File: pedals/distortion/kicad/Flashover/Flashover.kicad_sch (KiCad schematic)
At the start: 0 parts

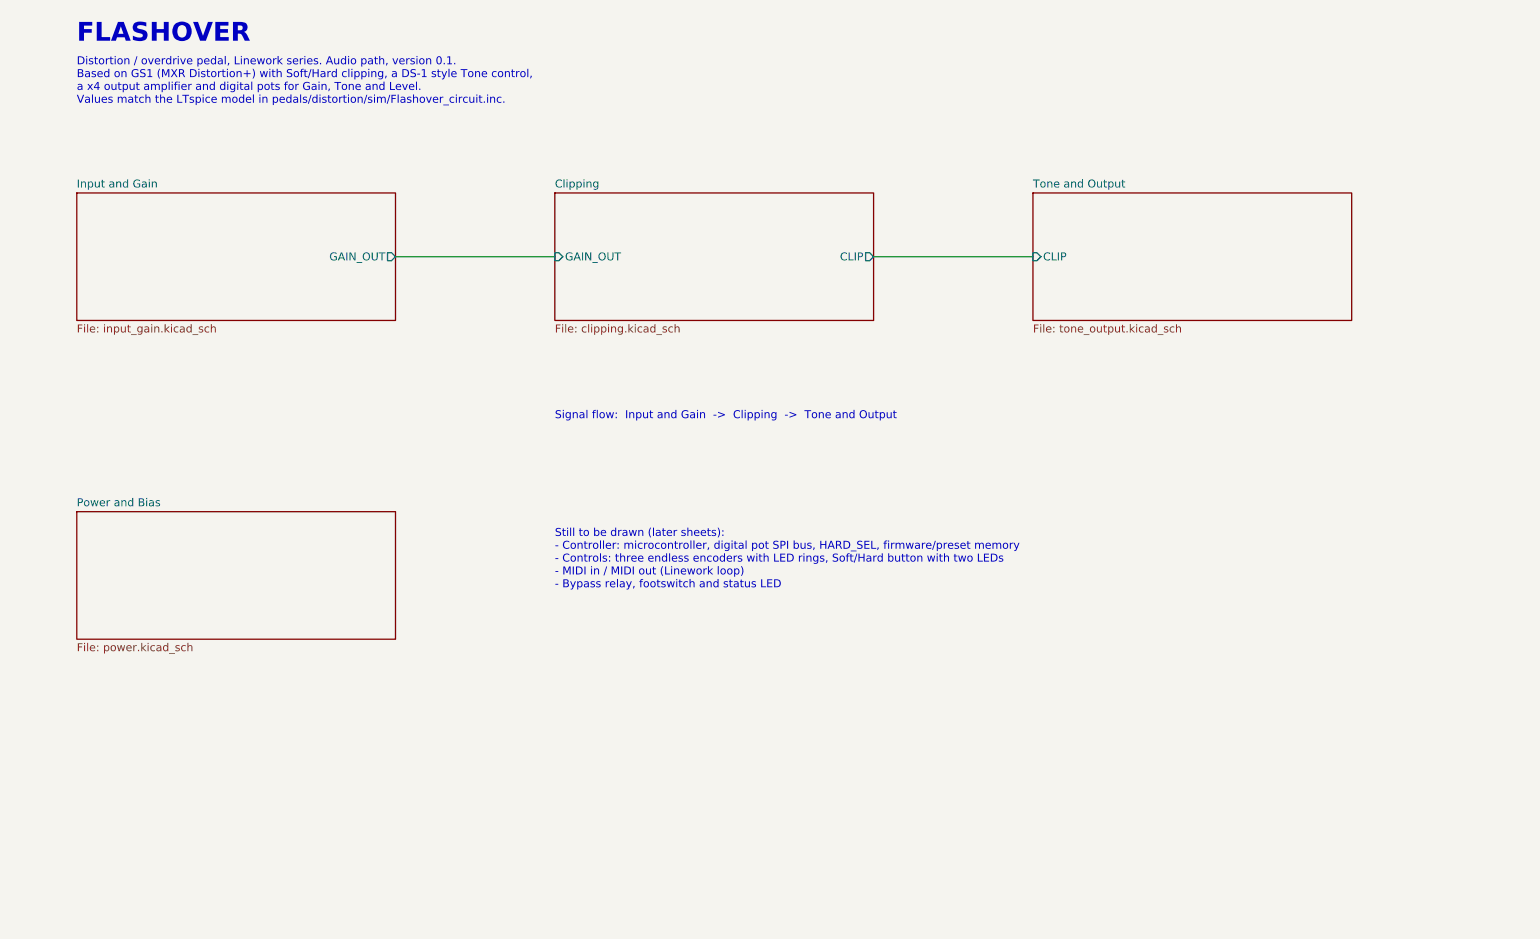
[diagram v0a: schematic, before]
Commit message: Add Flashover controller and digital pot sheets
Controller sheet: RP2040 with 3.3V regulator, 2 MB QSPI flash, 12 MHz
crystal and SWD header, plus a GPIO plan for the sheets still to come.
Digital Pots sheet: control side of three MCP45HV51 I2C pots with
pull-ups. RV1-RV3 on the audio sheets become the pot units of U7-U9
(new two-unit MCP45HV51 symbol in the shared library). ERC clean.

Co-Authored-By: Claude Opus 5.5 <noreply@anthropic.com>
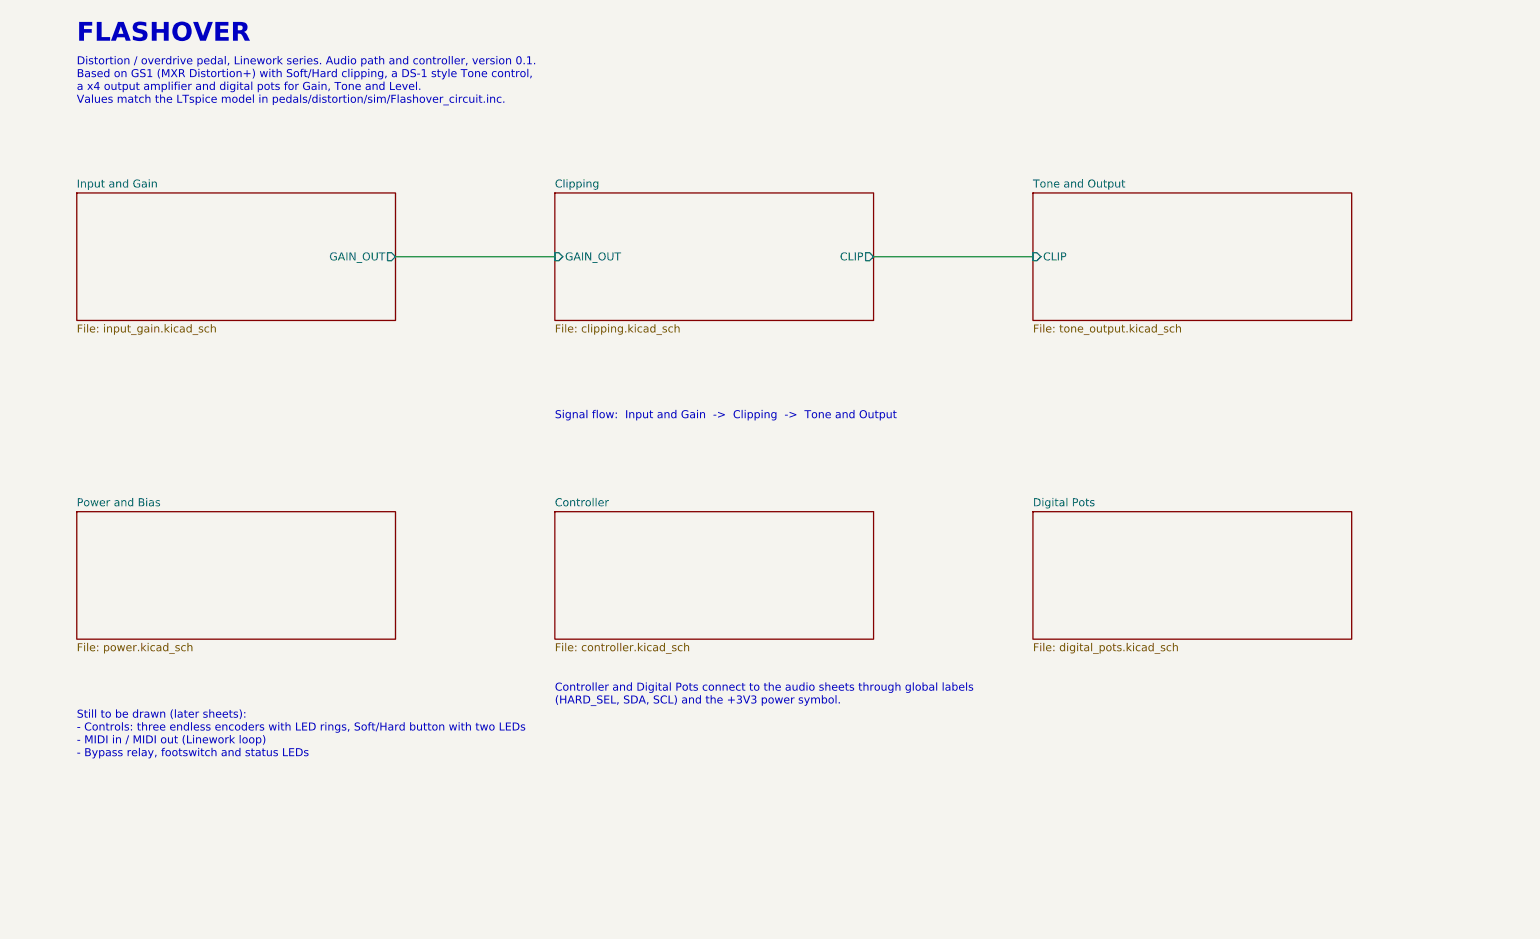
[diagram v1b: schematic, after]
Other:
- added sheet Controller (controller.kicad_sch)
- added sheet Digital Pots (digital_pots.kicad_sch)
- note added: "Controller and Digital Pots connect to the audio sheets through global labels (HARD_SEL, SDA, SCL) and the +3V3 power symbol."
- note added: "Distortion / overdrive pedal, Linework series. Audio path and controller, version 0.1. Based on GS1 (MXR Distortion+) with Soft/Hard clipping, a DS-1 style Tone control, a x4 output amplifier and digital pots for Gain, Tone and Level. Values match the LTspice model in pedals/distortion/sim/Flashover_circuit.inc."
- note added: "Still to be drawn (later sheets): - Controls: three endless encoders with LED rings, Soft/Hard button with two LEDs - MIDI in / MIDI out (Linework loop) - Bypass relay, footswitch and status LEDs"
- note removed: "Distortion / overdrive pedal, Linework series. Audio path, version 0.1. Based on GS1 (MXR Distortion+) with Soft/Hard clipping, a DS-1 style Tone control, a x4 output amplifier and digital pots for Gain, Tone and Level. Values match the LTspice model in pedals/distortion/sim/Flashover_circuit.inc."
- note removed: "Still to be drawn (later sheets): - Controller: microcontroller, digital pot SPI bus, HARD_SEL, firmware/preset memory - Controls: three endless encoders with LED rings, Soft/Hard button with two LEDs - MIDI in / MIDI out (Linework loop) - Bypass relay, footswitch and status LED"
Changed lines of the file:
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@@
 		(effects (font (size 3 3) (bold yes)) (justify left))
 	)
-	(text "Distortion / overdrive pedal, Linework series. Audio path, version 0.1.\nBased on GS1 (MXR Distortion+) with Soft/Hard clipping, a DS-1 style Tone control,\na x4 output amplifier and digital pots for Gain, Tone and Level.\nValues match the LTspice model in pedals/distortion/sim/Flashover_circuit.inc."
+	(text "Distortion / overdrive pedal, Linework series. Audio path and controller, version 0.1.\nBased on GS1 (MXR Distortion+) with Soft/Hard clipping, a DS-1 style Tone control,\na x4 output amplifier and digital pots for Gain, Tone and Level.\nValues match the LTspice model in pedals/distortion/sim/Flashover_circuit.inc."
 		(exclude_from_sim no)
 		(at 40.64 45.72 0)
@@
 		(effects (font (size 1.27 1.27)) (justify left))
 	)
-	(text "Still to be drawn (later sheets):\n- Controller: microcontroller, digital pot SPI bus, HARD_SEL, firmware/preset memory\n- Controls: three endless encoders with LED rings, Soft/Hard button with two LEDs\n- MIDI in / MIDI out (Linework loop)\n- Bypass relay, footswitch and status LED"
-		(exclude_from_sim no)
-		(at 116.84 121.92 0)
+	(text "Controller and Digital Pots connect to the audio sheets through global labels\n(HARD_SEL, SDA, SCL) and the +3V3 power symbol."
+		(exclude_from_sim no)
+		(at 116.84 143.51 0)
+		(effects (font (size 1.27 1.27)) (justify left))
+	)
+	(text "Still to be drawn (later sheets):\n- Controls: three endless encoders with LED rings, Soft/Hard button with two LEDs\n- MIDI in / MIDI out (Linework loop)\n- Bypass relay, footswitch and status LEDs"
+		(exclude_from_sim no)
+		(at 40.64 149.86 0)
 		(effects (font (size 1.27 1.27)) (justify left))
 	)
@@
 		(instances
 			(project "Flashover"
-				(path "/c1c20152-b132-4e14-97dc-1ac24480e45d"
+				(path "/37bda491-c0dc-4d48-acdf-49df4f139bb0"
 					(page "2")
 				)
@@
 		(instances
 			(project "Flashover"
-				(path "/c1c20152-b132-4e14-97dc-1ac24480e45d"
+				(path "/37bda491-c0dc-4d48-acdf-49df4f139bb0"
 					(page "3")
 				)
@@
 		(instances
 			(project "Flashover"
-				(path "/c1c20152-b132-4e14-97dc-1ac24480e45d"
+				(path "/37bda491-c0dc-4d48-acdf-49df4f139bb0"
 					(page "4")
 				)
@@
 		(instances
 			(project "Flashover"
-				(path "/c1c20152-b132-4e14-97dc-1ac24480e45d"
+				(path "/37bda491-c0dc-4d48-acdf-49df4f139bb0"
 					(page "5")
 				)
 			)
+		)
+	)
+	(sheet
+		(at 116.84 114.3)
+		(size 50.8 20.32)
+		(exclude_from_sim no)
+		(in_bom yes)
+		(on_board yes)
+		(dnp no)
+		(fields_autoplaced yes)
+		(stroke
+			(width 0.1524)
+			(type solid)
+		)
+		(fill
+			(color 0 0 0 0.0000)
+		)
+		(property "Sheetname" "Controller"
+			(at 116.84 113.5884 0)
+			(show_name no)
+			(do_not_autoplace no)
+			(effects (font (size 1.27 1.27)) (justify left bottom))
+		)
+		(property "Sheetfile" "controller.kicad_sch"
+			(at 116.84 135.2046 0)
+			(show_name no)
+			(do_not_autoplace no)
+			(effects (font (size 1.27 1.27)) (justify left top))
+		)
+		(instances
+			(project "Flashover"
+				(path "/37bda491-c0dc-4d48-acdf-49df4f139bb0"
+					(page "6")
+				)
+			)
+		)
+	)
+	(sheet
+		(at 193.04 114.3)
+		(size 50.8 20.32)
+		(exclude_from_sim no)
+		(in_bom yes)
+		(on_board yes)
+		(dnp no)
+		(fields_autoplaced yes)
+		(stroke
+			(width 0.1524)
+			(type solid)
+		)
+		(fill
+			(color 0 0 0 0.0000)
+		)
+		(property "Sheetname" "Digital Pots"
+			(at 193.04 113.5884 0)
+			(show_name no)
+			(do_not_autoplace no)
+			(effects (font (size 1.27 1.27)) (justify left bottom))
+		)
+		(property "Sheetfile" "digital_pots.kicad_sch"
+			(at 193.04 135.2046 0)
+			(show_name no)
+			(do_not_autoplace no)
+			(effects (font (size 1.27 1.27)) (justify left top))
+		)
+		(instances
+			(project "Flashover"
+				(path "/37bda491-c0dc-4d48-acdf-49df4f139bb0"
+					(page "7")
+				)
+			)

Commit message: Add Flashover controls and LED ring sheets
Controls sheet: three PEC11R encoders with push switches (pull-ups and
RC filtering) and the Soft/Hard button. LED Rings sheet: IS31FL3236A
driving three 11-LED rings plus Soft, Hard and On LEDs, on its own I2C
bus. Controller sheet wires the new GPIOs; the 5V regulator becomes an
L7805 for the LED load. ERC clean.

Co-Authored-By: Claude Opus 5.5 <noreply@anthropic.com>
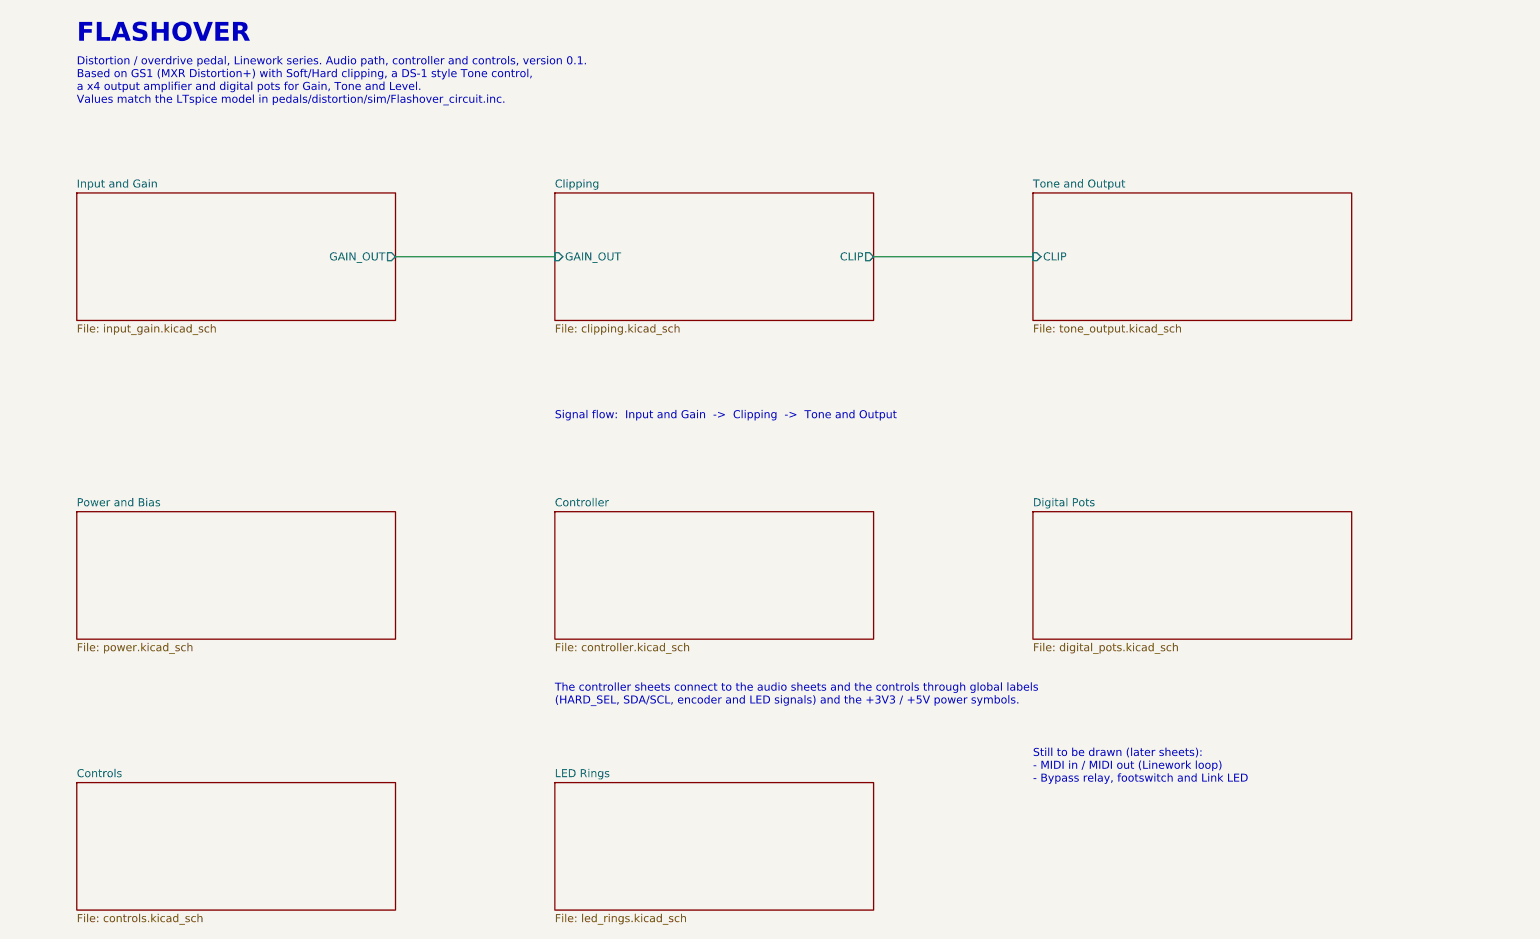
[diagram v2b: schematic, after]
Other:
- added sheet Controls (controls.kicad_sch)
- added sheet LED Rings (led_rings.kicad_sch)
- note added: "Distortion / overdrive pedal, Linework series. Audio path, controller and controls, version 0.1. Based on GS1 (MXR Distortion+) with Soft/Hard clipping, a DS-1 style Tone control, a x4 output amplifier and digital pots for Gain, Tone and Level. Values match the LTspice model in pedals/distortion/sim/Flashover_circuit.inc."
- note added: "Still to be drawn (later sheets): - MIDI in / MIDI out (Linework loop) - Bypass relay, footswitch and Link LED"
- note added: "The controller sheets connect to the audio sheets and the controls through global labels (HARD_SEL, SDA/SCL, encoder and LED signals) and the +3V3 / +5V power symbols."
- note removed: "Controller and Digital Pots connect to the audio sheets through global labels (HARD_SEL, SDA, SCL) and the +3V3 power symbol."
- note removed: "Distortion / overdrive pedal, Linework series. Audio path and controller, version 0.1. Based on GS1 (MXR Distortion+) with Soft/Hard clipping, a DS-1 style Tone control, a x4 output amplifier and digital pots for Gain, Tone and Level. Values match the LTspice model in pedals/distortion/sim/Flashover_circuit.inc."
- note removed: "Still to be drawn (later sheets): - Controls: three endless encoders with LED rings, Soft/Hard button with two LEDs - MIDI in / MIDI out (Linework loop) - Bypass relay, footswitch and status LEDs"
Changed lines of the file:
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@@
 	(title_block
 		(title "Flashover")
-		(date "2026-10-08")
+		(date "2026-10-09")
 		(rev "0.1")
 		(company "GreywireStudio")
@@
 		(effects (font (size 3 3) (bold yes)) (justify left))
 	)
-	(text "Distortion / overdrive pedal, Linework series. Audio path and controller, version 0.1.\nBased on GS1 (MXR Distortion+) with Soft/Hard clipping, a DS-1 style Tone control,\na x4 output amplifier and digital pots for Gain, Tone and Level.\nValues match the LTspice model in pedals/distortion/sim/Flashover_circuit.inc."
+	(text "Distortion / overdrive pedal, Linework series. Audio path, controller and controls, version 0.1.\nBased on GS1 (MXR Distortion+) with Soft/Hard clipping, a DS-1 style Tone control,\na x4 output amplifier and digital pots for Gain, Tone and Level.\nValues match the LTspice model in pedals/distortion/sim/Flashover_circuit.inc."
 		(exclude_from_sim no)
 		(at 40.64 45.72 0)
@@
 		(effects (font (size 1.27 1.27)) (justify left))
 	)
-	(text "Controller and Digital Pots connect to the audio sheets through global labels\n(HARD_SEL, SDA, SCL) and the +3V3 power symbol."
+	(text "The controller sheets connect to the audio sheets and the controls through global labels\n(HARD_SEL, SDA/SCL, encoder and LED signals) and the +3V3 / +5V power symbols."
 		(exclude_from_sim no)
 		(at 116.84 143.51 0)
 		(effects (font (size 1.27 1.27)) (justify left))
 	)
-	(text "Still to be drawn (later sheets):\n- Controls: three endless encoders with LED rings, Soft/Hard button with two LEDs\n- MIDI in / MIDI out (Linework loop)\n- Bypass relay, footswitch and status LEDs"
-		(exclude_from_sim no)
-		(at 40.64 149.86 0)
+	(text "Still to be drawn (later sheets):\n- MIDI in / MIDI out (Linework loop)\n- Bypass relay, footswitch and Link LED"
+		(exclude_from_sim no)
+		(at 193.04 154.94 0)
 		(effects (font (size 1.27 1.27)) (justify left))
 	)
@@
 		(instances
 			(project "Flashover"
-				(path "/37bda491-c0dc-4d48-acdf-49df4f139bb0"
+				(path "/ea9f0b88-0903-4174-9c8e-623c203001c6"
 					(page "2")
 				)
@@
 		(instances
 			(project "Flashover"
-				(path "/37bda491-c0dc-4d48-acdf-49df4f139bb0"
+				(path "/ea9f0b88-0903-4174-9c8e-623c203001c6"
 					(page "3")
 				)
@@
 		(instances
 			(project "Flashover"
-				(path "/37bda491-c0dc-4d48-acdf-49df4f139bb0"
+				(path "/ea9f0b88-0903-4174-9c8e-623c203001c6"
 					(page "4")
 				)
@@
 		(instances
 			(project "Flashover"
-				(path "/37bda491-c0dc-4d48-acdf-49df4f139bb0"
+				(path "/ea9f0b88-0903-4174-9c8e-623c203001c6"
 					(page "5")
 				)
@@
 		(instances
 			(project "Flashover"
-				(path "/37bda491-c0dc-4d48-acdf-49df4f139bb0"
+				(path "/ea9f0b88-0903-4174-9c8e-623c203001c6"
 					(page "6")
 				)
@@
 		(instances
 			(project "Flashover"
-				(path "/37bda491-c0dc-4d48-acdf-49df4f139bb0"
+				(path "/ea9f0b88-0903-4174-9c8e-623c203001c6"
 					(page "7")
 				)
 			)
+		)
+	)
+	(sheet
+		(at 40.64 157.48)
+		(size 50.8 20.32)
+		(exclude_from_sim no)
+		(in_bom yes)
+		(on_board yes)
+		(dnp no)
+		(fields_autoplaced yes)
+		(stroke
+			(width 0.1524)
+			(type solid)
+		)
+		(fill
+			(color 0 0 0 0.0000)
+		)
+		(property "Sheetname" "Controls"
+			(at 40.64 156.7684 0)
+			(show_name no)
+			(do_not_autoplace no)
+			(effects (font (size 1.27 1.27)) (justify left bottom))
+		)
+		(property "Sheetfile" "controls.kicad_sch"
+			(at 40.64 178.3846 0)
+			(show_name no)
+			(do_not_autoplace no)
+			(effects (font (size 1.27 1.27)) (justify left top))
+		)
+		(instances
+			(project "Flashover"
+				(path "/ea9f0b88-0903-4174-9c8e-623c203001c6"
+					(page "8")
+				)
+			)
+		)
+	)
+	(sheet
+		(at 116.84 157.48)
+		(size 50.8 20.32)
+		(exclude_from_sim no)
+		(in_bom yes)
+		(on_board yes)
+		(dnp no)
+		(fields_autoplaced yes)
+		(stroke
+			(width 0.1524)
+			(type solid)
+		)
+		(fill
+			(color 0 0 0 0.0000)
+		)
+		(property "Sheetname" "LED Rings"
+			(at 116.84 156.7684 0)
+			(show_name no)
+			(do_not_autoplace no)
+			(effects (font (size 1.27 1.27)) (justify left bottom))
+		)
+		(property "Sheetfile" "led_rings.kicad_sch"
+			(at 116.84 178.3846 0)
+			(show_name no)
+			(do_not_autoplace no)
+			(effects (font (size 1.27 1.27)) (justify left top))
+		)
+		(instances
+			(project "Flashover"
+				(path "/ea9f0b88-0903-4174-9c8e-623c203001c6"
+					(page "9")
+				)
+			)
